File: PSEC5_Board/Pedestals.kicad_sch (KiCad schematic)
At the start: 48 parts, among them J11 Conn_Coaxial, J2 Conn_Coaxial, J3 Conn_Coaxial, J4 Conn_Coaxial, J5 Conn_Coaxial, J6 Conn_Coaxial, J7 Conn_Coaxial, J8 Conn_Coaxial

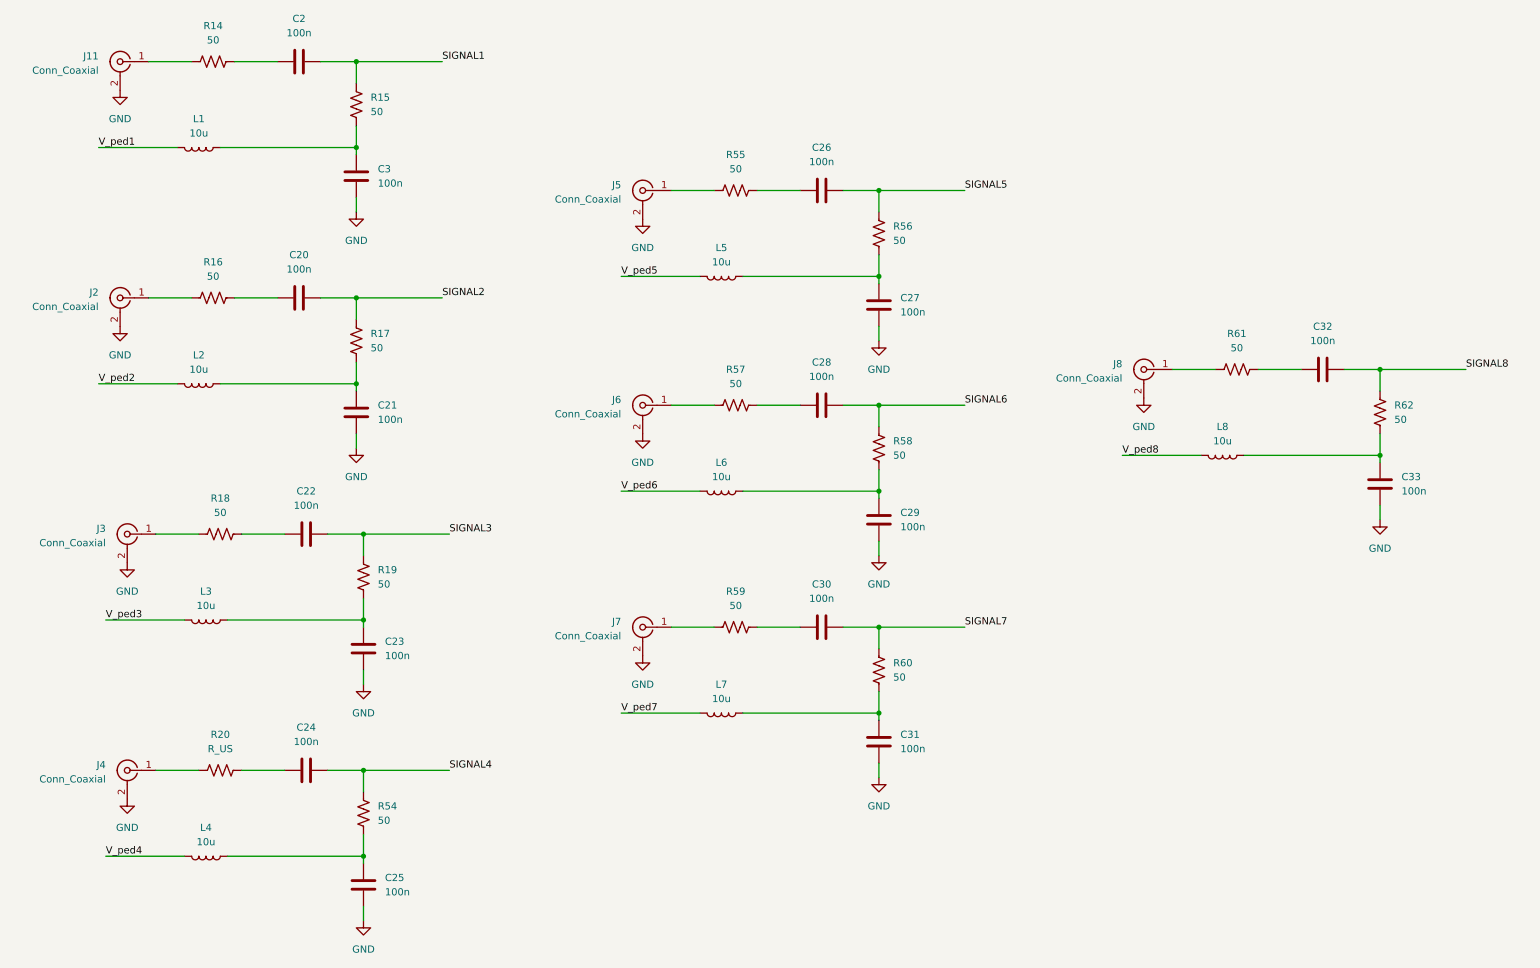
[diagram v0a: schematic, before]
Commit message: DUT - Fixed ADC Driver
Passes ERC - SAMTEC connections still needs to be matched.
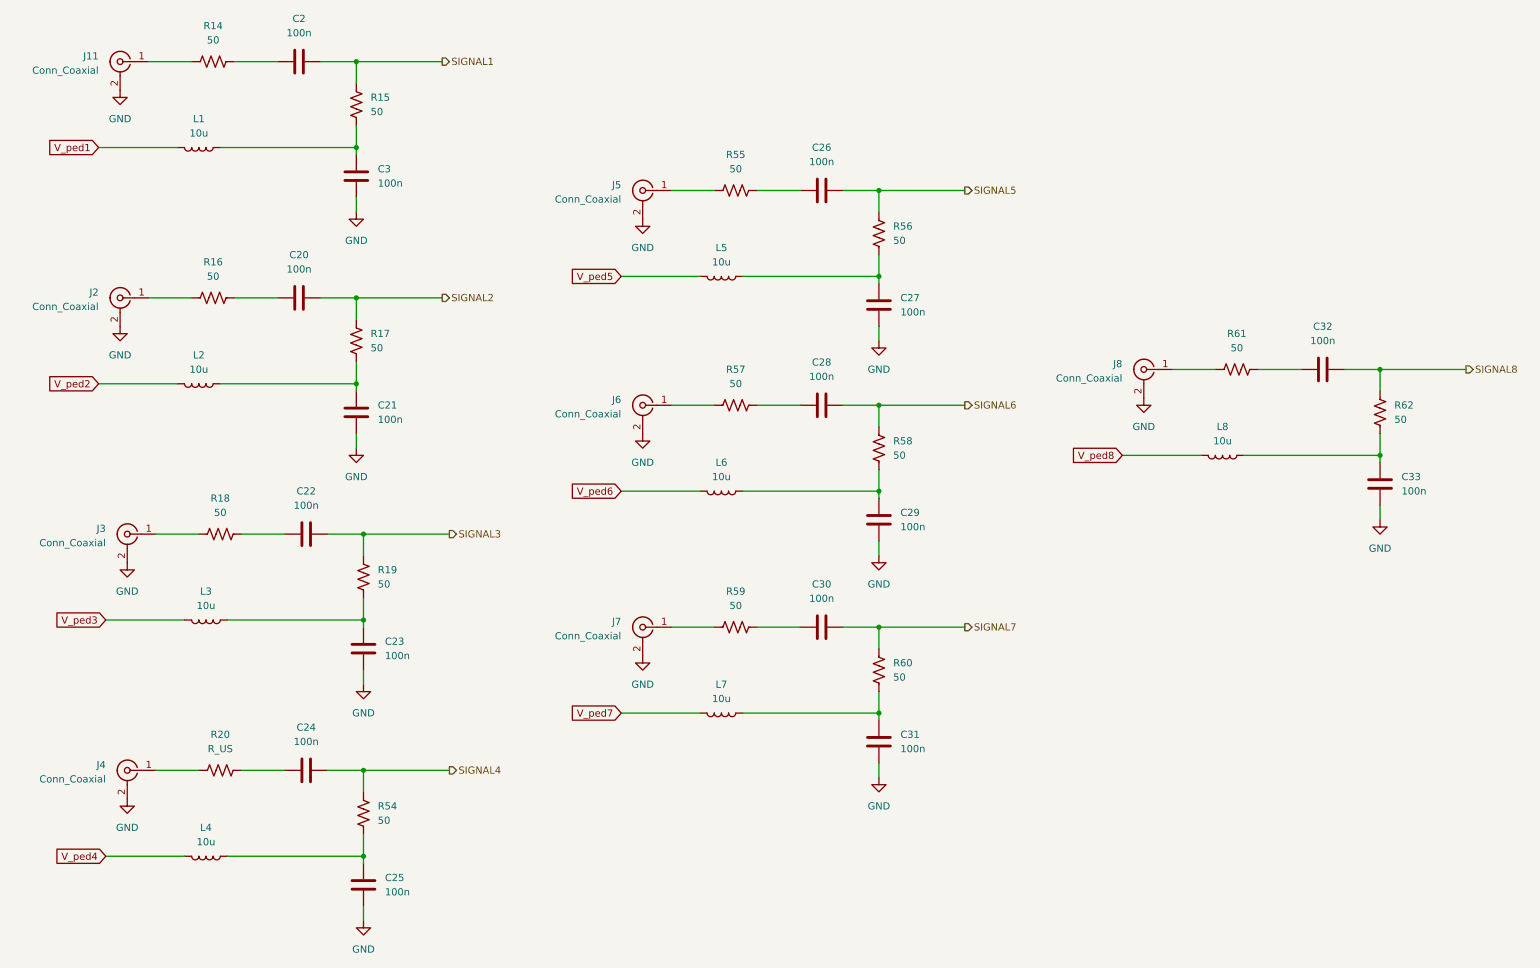
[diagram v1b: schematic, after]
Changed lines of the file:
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@@
 		)
 	)
-	(label "V_ped6"
-		(at 121.92 101.6 0)
-		(fields_autoplaced yes)
-		(effects
-			(font
-				(size 1.27 1.27)
-			)
-			(justify left bottom)
-		)
-	)
-	(label "SIGNAL1"
+	(global_label "V_ped7"
+		(shape input)
+		(at 121.92 140.97 180)
+		(fields_autoplaced yes)
+		(effects
+			(font
+				(size 1.27 1.27)
+			)
+			(justify right)
+		)
+		(property "Intersheetrefs" "${INTERSHEET_REFS}"
+			(at 112.2825 140.97 0)
+			(effects
+				(font
+					(size 1.27 1.27)
+				)
+				(justify right)
+				(hide yes)
+			)
+		)
+	)
+	(global_label "V_ped1"
+		(shape input)
+		(at 29.21 40.64 180)
+		(fields_autoplaced yes)
+		(effects
+			(font
+				(size 1.27 1.27)
+			)
+			(justify right)
+		)
+		(property "Intersheetrefs" "${INTERSHEET_REFS}"
+			(at 19.5725 40.64 0)
+			(effects
+				(font
+					(size 1.27 1.27)
+				)
+				(justify right)
+				(hide yes)
+			)
+		)
+	)
+	(global_label "V_ped5"
+		(shape input)
+		(at 121.92 63.5 180)
+		(fields_autoplaced yes)
+		(effects
+			(font
+				(size 1.27 1.27)
+			)
+			(justify right)
+		)
+		(property "Intersheetrefs" "${INTERSHEET_REFS}"
+			(at 112.2825 63.5 0)
+			(effects
+				(font
+					(size 1.27 1.27)
+				)
+				(justify right)
+				(hide yes)
+			)
+		)
+	)
+	(global_label "V_ped2"
+		(shape input)
+		(at 29.21 82.55 180)
+		(fields_autoplaced yes)
+		(effects
+			(font
+				(size 1.27 1.27)
+			)
+			(justify right)
+		)
+		(property "Intersheetrefs" "${INTERSHEET_REFS}"
+			(at 19.5725 82.55 0)
+			(effects
+				(font
+					(size 1.27 1.27)
+				)
+				(justify right)
+				(hide yes)
+			)
+		)
+	)
+	(global_label "V_ped6"
+		(shape input)
+		(at 121.92 101.6 180)
+		(fields_autoplaced yes)
+		(effects
+			(font
+				(size 1.27 1.27)
+			)
+			(justify right)
+		)
+		(property "Intersheetrefs" "${INTERSHEET_REFS}"
+			(at 112.2825 101.6 0)
+			(effects
+				(font
+					(size 1.27 1.27)
+				)
+				(justify right)
+				(hide yes)
+			)
+		)
+	)
+	(global_label "V_ped4"
+		(shape input)
+		(at 30.48 166.37 180)
+		(fields_autoplaced yes)
+		(effects
+			(font
+				(size 1.27 1.27)
+			)
+			(justify right)
+		)
+		(property "Intersheetrefs" "${INTERSHEET_REFS}"
+			(at 20.8425 166.37 0)
+			(effects
+				(font
+					(size 1.27 1.27)
+				)
+				(justify right)
+				(hide yes)
+			)
+		)
+	)
+	(global_label "V_ped3"
+		(shape input)
+		(at 30.48 124.46 180)
+		(fields_autoplaced yes)
+		(effects
+			(font
+				(size 1.27 1.27)
+			)
+			(justify right)
+		)
+		(property "Intersheetrefs" "${INTERSHEET_REFS}"
+			(at 20.8425 124.46 0)
+			(effects
+				(font
+					(size 1.27 1.27)
+				)
+				(justify right)
+				(hide yes)
+			)
+		)
+	)
+	(global_label "V_ped8"
+		(shape input)
+		(at 210.82 95.25 180)
+		(fields_autoplaced yes)
+		(effects
+			(font
+				(size 1.27 1.27)
+			)
+			(justify right)
+		)
+		(property "Intersheetrefs" "${INTERSHEET_REFS}"
+			(at 201.1825 95.25 0)
+			(effects
+				(font
+					(size 1.27 1.27)
+				)
+				(justify right)
+				(hide yes)
+			)
+		)
+	)
+	(hierarchical_label "SIGNAL7"
+		(shape output)
+		(at 182.88 125.73 0)
+		(fields_autoplaced yes)
+		(effects
+			(font
+				(size 1.27 1.27)
+			)
+			(justify left)
+		)
+	)
+	(hierarchical_label "SIGNAL4"
+		(shape output)
+		(at 91.44 151.13 0)
+		(fields_autoplaced yes)
+		(effects
+			(font
+				(size 1.27 1.27)
+			)
+			(justify left)
+		)
+	)
+	(hierarchical_label "SIGNAL3"
+		(shape output)
+		(at 91.44 109.22 0)
+		(fields_autoplaced yes)
+		(effects
+			(font
+				(size 1.27 1.27)
+			)
+			(justify left)
+		)
+	)
+	(hierarchical_label "SIGNAL5"
+		(shape output)
+		(at 182.88 48.26 0)
+		(fields_autoplaced yes)
+		(effects
+			(font
+				(size 1.27 1.27)
+			)
+			(justify left)
+		)
+	)
+	(hierarchical_label "SIGNAL2"
+		(shape output)
+		(at 90.17 67.31 0)
+		(fields_autoplaced yes)
+		(effects
+			(font
+				(size 1.27 1.27)
+			)
+			(justify left)
+		)
+	)
+	(hierarchical_label "SIGNAL6"
+		(shape output)
+		(at 182.88 86.36 0)
+		(fields_autoplaced yes)
+		(effects
+			(font
+				(size 1.27 1.27)
+			)
+			(justify left)
+		)
+	)
+	(hierarchical_label "SIGNAL8"
+		(shape output)
+		(at 271.78 80.01 0)
+		(fields_autoplaced yes)
+		(effects
+			(font
+				(size 1.27 1.27)
+			)
+			(justify left)
+		)
+	)
+	(hierarchical_label "SIGNAL1"
+		(shape output)
 		(at 90.17 25.4 0)
 		(fields_autoplaced yes)
@@
 				(size 1.27 1.27)
 			)
-			(justify left bottom)
-		)
-	)
-	(label "SIGNAL4"
-		(at 91.44 151.13 0)
-		(fields_autoplaced yes)
-		(effects
-			(font
-				(size 1.27 1.27)
-			)
-			(justify left bottom)
-		)
-	)
-	(label "SIGNAL2"
-		(at 90.17 67.31 0)
-		(fields_autoplaced yes)
-		(effects
-			(font
-				(size 1.27 1.27)
-			)
-			(justify left bottom)
-		)
-	)
-	(label "SIGNAL8"
-		(at 271.78 80.01 0)
-		(fields_autoplaced yes)
-		(effects
-			(font
-				(size 1.27 1.27)
-			)
-			(justify left bottom)
-		)
-	)
-	(label "SIGNAL5"
-		(at 182.88 48.26 0)
-		(fields_autoplaced yes)
-		(effects
-			(font
-				(size 1.27 1.27)
-			)
-			(justify left bottom)
-		)
-	)
-	(label "V_ped4"
-		(at 30.48 166.37 0)
-		(fields_autoplaced yes)
-		(effects
-			(font
-				(size 1.27 1.27)
-			)
-			(justify left bottom)
-		)
-	)
-	(label "V_ped5"
-		(at 121.92 63.5 0)
-		(fields_autoplaced yes)
-		(effects
-			(font
-				(size 1.27 1.27)
-			)
-			(justify left bottom)
-		)
-	)
-	(label "SIGNAL7"
-		(at 182.88 125.73 0)
-		(fields_autoplaced yes)
-		(effects
-			(font
-				(size 1.27 1.27)
-			)
-			(justify left bottom)
-		)
-	)
-	(label "V_ped8"
-		(at 210.82 95.25 0)
-		(fields_autoplaced yes)
-		(effects
-			(font
-				(size 1.27 1.27)
-			)
-			(justify left bottom)
-		)
-	)
-	(label "SIGNAL6"
-		(at 182.88 86.36 0)
-		(fields_autoplaced yes)
-		(effects
-			(font
-				(size 1.27 1.27)
-			)
-			(justify left bottom)
-		)
-	)
-	(label "V_ped1"
-		(at 29.21 40.64 0)
-		(fields_autoplaced yes)
-		(effects
-			(font
-				(size 1.27 1.27)
-			)
-			(justify left bottom)
-		)
-	)
-	(label "SIGNAL3"
-		(at 91.44 109.22 0)
-		(fields_autoplaced yes)
-		(effects
-			(font
-				(size 1.27 1.27)
-			)
-			(justify left bottom)
-		)
-	)
-	(label "V_ped3"
-		(at 30.48 124.46 0)
-		(fields_autoplaced yes)
-		(effects
-			(font
-				(size 1.27 1.27)
-			)
-			(justify left bottom)
-		)
-	)
-	(label "V_ped7"
-		(at 121.92 140.97 0)
-		(fields_autoplaced yes)
-		(effects
-			(font
-				(size 1.27 1.27)
-			)
-			(justify left bottom)
-		)
-	)
-	(label "V_ped2"
-		(at 29.21 82.55 0)
-		(fields_autoplaced yes)
-		(effects
-			(font
-				(size 1.27 1.27)
-			)
-			(justify left bottom)
-		)
-	)
+			(justify left)
+		)
+	)

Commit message: Added Footprints to Schematic
Added footprints to schematic, should be able to now update the layout design and have all nets be present
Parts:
- C2, C20, C21, C22, C23, C24, C25, C26, C27, C28, C29, C3, C30, C31, C32, C33: footprint (none) -> Capacitor_SMD:C_0603_1608Metric
- L1, L2, L3, L4, L5, L6, L7, L8: footprint (none) -> Inductor_SMD:L_0603_1608Metric_Pad1.05x0.95mm_HandSolder
- R14, R15, R16, R17, R18, R19, R20, R54, R55, R56, R57, R58, R59, R60, R61, R62: footprint (none) -> Resistor_SMD:R_0603_1608Metric
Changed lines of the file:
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@@
 			)
 		)
-		(property "Footprint" ""
+		(property "Footprint" "Capacitor_SMD:C_0603_1608Metric"
 			(at 77.1652 175.26 0)
 			(effects
@@
 			)
 		)
-		(property "Footprint" ""
+		(property "Footprint" "Resistor_SMD:R_0603_1608Metric"
 			(at 141.986 126.746 90)
 			(effects
@@
 			)
 		)
-		(property "Footprint" ""
+		(property "Footprint" "Capacitor_SMD:C_0603_1608Metric"
 			(at 62.23 110.1852 0)
 			(effects
@@
 			)
 		)
-		(property "Footprint" ""
+		(property "Footprint" "Capacitor_SMD:C_0603_1608Metric"
 			(at 168.6052 72.39 0)
 			(effects
@@
 			)
 		)
-		(property "Footprint" ""
+		(property "Footprint" "Capacitor_SMD:C_0603_1608Metric"
 			(at 62.23 152.0952 0)
 			(effects
@@
 			)
 		)
-		(property "Footprint" ""
+		(property "Footprint" "Capacitor_SMD:C_0603_1608Metric"
 			(at 60.96 26.3652 0)
 			(effects
@@
 			)
 		)
-		(property "Footprint" ""
+		(property "Footprint" "Capacitor_SMD:C_0603_1608Metric"
 			(at 75.8952 91.44 0)
 			(effects
@@
 			)
 		)
-		(property "Footprint" ""
+		(property "Footprint" "Resistor_SMD:R_0603_1608Metric"
 			(at 255.524 87.376 90)
 			(effects
@@
 			)
 		)
-		(property "Footprint" ""
+		(property "Footprint" "Capacitor_SMD:C_0603_1608Metric"
 			(at 153.67 49.2252 0)
 			(effects
@@
 			)
 		)
-		(property "Footprint" ""
+		(property "Footprint" "Capacitor_SMD:C_0603_1608Metric"
 			(at 242.57 80.9752 0)
 			(effects
@@
 			)
 		)
-		(property "Footprint" ""
+		(property "Footprint" "Resistor_SMD:R_0603_1608Metric"
 			(at 50.546 152.146 90)
 			(effects
@@
 			)
 		)
-		(property "Footprint" ""
+		(property "Footprint" "Resistor_SMD:R_0603_1608Metric"
 			(at 141.986 49.276 90)
 			(effects
@@
 			)
 		)
-		(property "Footprint" ""
+		(property "Footprint" "Resistor_SMD:R_0603_1608Metric"
 			(at 49.276 68.326 90)
 			(effects
@@
 			)
 		)
-		(property "Footprint" ""
+		(property "Footprint" "Inductor_SMD:L_0603_1608Metric_Pad1.05x0.95mm_HandSolder"
 			(at 46.99 82.55 0)
 			(effects
@@
 			)
 		)
-		(property "Footprint" ""
+		(property "Footprint" "Inductor_SMD:L_0603_1608Metric_Pad1.05x0.95mm_HandSolder"
 			(at 139.7 140.97 0)
 			(effects
@@
 			)
 		)
-		(property "Footprint" ""
+		(property "Footprint" "Capacitor_SMD:C_0603_1608Metric"
 			(at 77.1652 133.35 0)
 			(effects
@@
 			)
 		)
-		(property "Footprint" ""
+		(property "Footprint" "Resistor_SMD:R_0603_1608Metric"
 			(at 73.914 32.766 90)
 			(effects
@@
 			)
 		)
-		(property "Footprint" ""
+		(property "Footprint" "Resistor_SMD:R_0603_1608Metric"
 			(at 141.986 87.376 90)
 			(effects
@@
 			)
 		)
-		(property "Footprint" ""
+		(property "Footprint" "Resistor_SMD:R_0603_1608Metric"
 			(at 75.184 158.496 90)
 			(effects
@@
 			)
 		)
-		(property "Footprint" ""
+		(property "Footprint" "Resistor_SMD:R_0603_1608Metric"
 			(at 73.914 74.676 90)
 			(effects
@@
 			)
 		)
-		(property "Footprint" ""
+		(property "Footprint" "Resistor_SMD:R_0603_1608Metric"
 			(at 75.184 116.586 90)
 			(effects
@@
 			)
 		)
-		(property "Footprint" ""
+		(property "Footprint" "Inductor_SMD:L_0603_1608Metric_Pad1.05x0.95mm_HandSolder"
 			(at 139.7 63.5 0)
 			(effects
@@
 			)
 		)
-		(property "Footprint" ""
+		(property "Footprint" "Resistor_SMD:R_0603_1608Metric"
 			(at 166.624 133.096 90)
 			(effects
@@
 			)
 		)
-		(property "Footprint" ""
+		(property "Footprint" "Capacitor_SMD:C_0603_1608Metric"
 			(at 168.6052 110.49 0)
 			(effects
@@
 			)
 		)
-		(property "Footprint" ""
+		(property "Footprint" "Capacitor_SMD:C_0603_1608Metric"
 			(at 153.67 126.6952 0)
 			(effects
@@
 			)
 		)
-		(property "Footprint" ""
+		(property "Footprint" "Inductor_SMD:L_0603_1608Metric_Pad1.05x0.95mm_HandSolder"
 			(at 48.26 166.37 0)
 			(effects
@@
 			)
 		)
-		(property "Footprint" ""
+		(property "Footprint" "Inductor_SMD:L_0603_1608Metric_Pad1.05x0.95mm_HandSolder"
 			(at 46.99 40.64 0)
 			(effects
@@
 			)
 		)
-		(property "Footprint" ""
+		(property "Footprint" "Inductor_SMD:L_0603_1608Metric_Pad1.05x0.95mm_HandSolder"
 			(at 48.26 124.46 0)
 			(effects
@@
 			)
 		)
-		(property "Footprint" ""
+		(property "Footprint" "Capacitor_SMD:C_0603_1608Metric"
 			(at 153.67 87.3252 0)
 			(effects
@@
 			)
 		)
-		(property "Footprint" ""
+		(property "Footprint" "Capacitor_SMD:C_0603_1608Metric"
 			(at 75.8952 49.53 0)
 			(effects
@@
 			)
 		)
-		(property "Footprint" ""
+		(property "Footprint" "Inductor_SMD:L_0603_1608Metric_Pad1.05x0.95mm_HandSolder"
 			(at 139.7 101.6 0)
 			(effects
@@
 			)
 		)
-		(property "Footprint" ""
+		(property "Footprint" "Capacitor_SMD:C_0603_1608Metric"
 			(at 168.6052 149.86 0)
 			(effects
@@
 			)
 		)
-		(property "Footprint" ""
+		(property "Footprint" "Resistor_SMD:R_0603_1608Metric"
 			(at 230.886 81.026 90)
 			(effects
@@
 			)
 		)
-		(property "Footprint" ""
+		(property "Footprint" "Resistor_SMD:R_0603_1608Metric"
 			(at 166.624 93.726 90)
 			(effects
@@
 			)
 		)
-		(property "Footprint" ""
+		(property "Footprint" "Capacitor_SMD:C_0603_1608Metric"
 			(at 60.96 68.2752 0)
 			(effects
@@
 			)
 		)
-		(property "Footprint" ""
+		(property "Footprint" "Capacitor_SMD:C_0603_1608Metric"
 			(at 257.5052 104.14 0)
 			(effects
@@
 			)
 		)
-		(property "Footprint" ""
+		(property "Footprint" "Resistor_SMD:R_0603_1608Metric"
 			(at 166.624 55.626 90)
 			(effects
@@
 			)
 		)
-		(property "Footprint" ""
+		(property "Footprint" "Inductor_SMD:L_0603_1608Metric_Pad1.05x0.95mm_HandSolder"
 			(at 228.6 95.25 0)
 			(effects
@@
 			)
 		)
-		(property "Footprint" ""
+		(property "Footprint" "Resistor_SMD:R_0603_1608Metric"
 			(at 50.546 110.236 90)
 			(effects
@@
 			)
 		)
-		(property "Footprint" ""
+		(property "Footprint" "Resistor_SMD:R_0603_1608Metric"
 			(at 49.276 26.416 90)
 			(effects
